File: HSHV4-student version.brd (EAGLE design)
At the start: 55 x 55 mm, 34 parts, among them IC1 DS3231, IC4 IO_EXPANDER, K1 PIN20X2, Q1 MOSFET-NCHANNEL2N7000, Q2 MOSFET-NCHANNEL2N7000, U1 256K_EEPROM

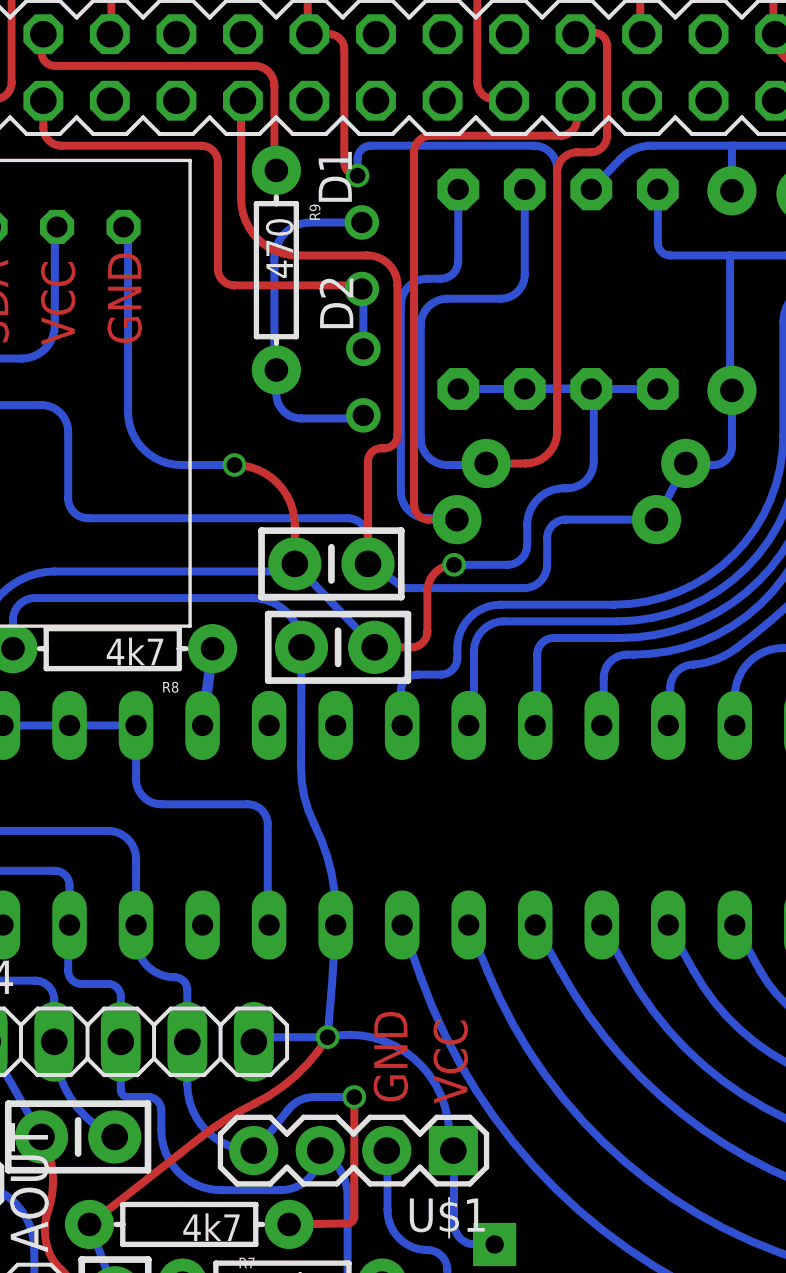
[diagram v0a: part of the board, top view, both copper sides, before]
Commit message: Increased size of via's for easier soldering
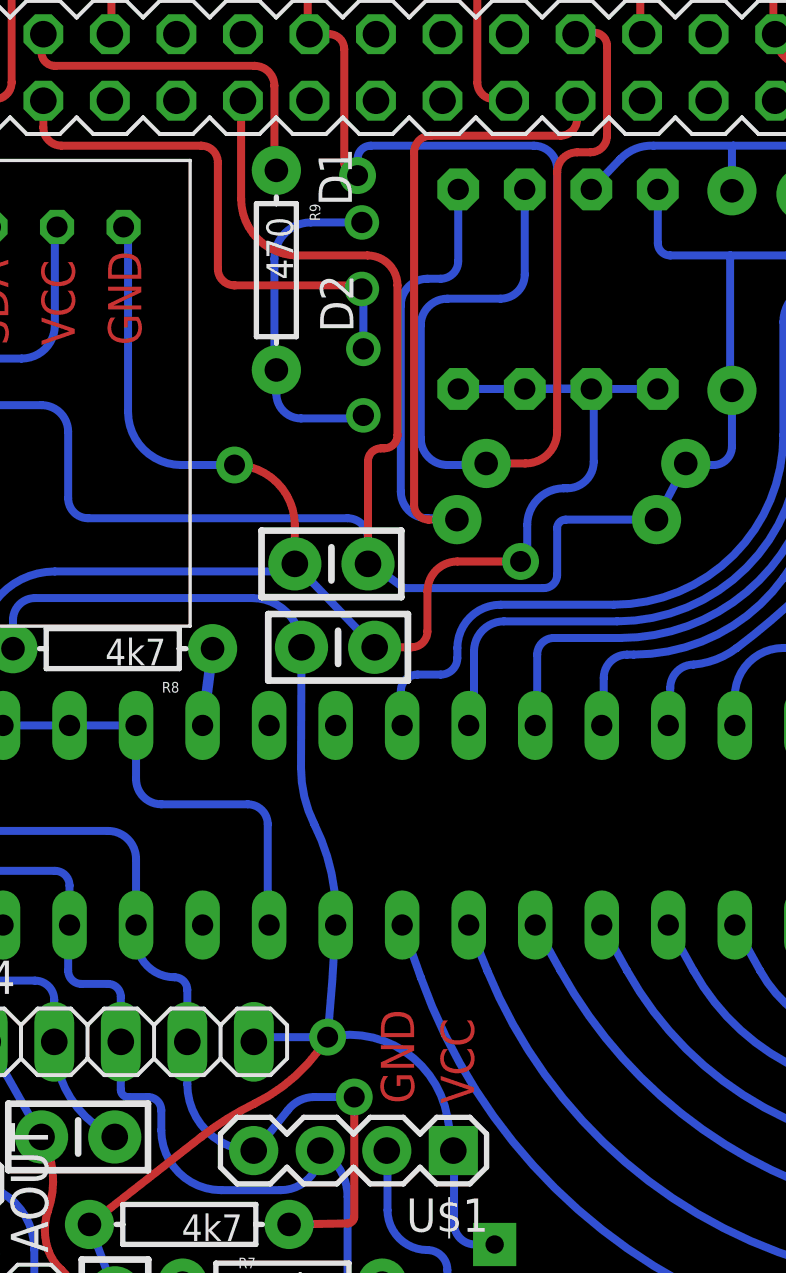
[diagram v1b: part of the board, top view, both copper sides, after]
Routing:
- net GND: track 297.6 -> 298.3 mm
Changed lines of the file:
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@@
 <setting verticaltext="up"/>
 </settings>
-<grid distance="0.01" unitdist="inch" unit="inch" style="lines" multiple="8" display="yes" altdistance="0.005" altunitdist="inch" altunit="inch"/>
+<grid distance="0.01" unitdist="inch" unit="mm" style="lines" multiple="8" display="yes" altdistance="0.005" altunitdist="inch" altunit="mm"/>
 <layers>
 <layer number="1" name="Top" color="4" fill="1" visible="yes" active="yes"/>
@@
 <text x="17.272" y="40.894" size="1.27" layer="1" rot="R90">VCC</text>
 <text x="19.812" y="40.894" size="1.27" layer="1" rot="R90">GND</text>
-<text x="32.258" y="11.938" size="1.27" layer="1" rot="R90">VCC</text>
-<text x="29.972" y="11.938" size="1.27" layer="1" rot="R90">GND</text>
+<text x="32.512" y="11.938" size="1.27" layer="1" rot="R90">VCC</text>
+<text x="30.226" y="11.938" size="1.27" layer="1" rot="R90">GND</text>
 </plain>
 <attributes>
@@
 <param name="rlMinPadBottom" value="10mil"/>
 <param name="rlMaxPadBottom" value="20mil"/>
-<param name="rlMinViaOuter" value="6mil"/>
+<param name="rlMinViaOuter" value="12mil"/>
 <param name="rlMaxViaOuter" value="20mil"/>
-<param name="rlMinViaInner" value="6mil"/>
+<param name="rlMinViaInner" value="10mil"/>
 <param name="rlMaxViaInner" value="20mil"/>
 <param name="rlMinMicroViaOuter" value="4mil"/>
@@
 <wire x1="28.575" y1="48.514" x2="28.067" y2="48.006" width="0.3048" layer="16" curve="90"/>
 <wire x1="28.067" y1="48.006" x2="28.067" y2="47.371" width="0.3048" layer="16"/>
-<via x="28.067" y="47.371" extent="1-16" drill="0.6"/>
+<via x="28.067" y="47.371" extent="1-16" drill="0.8"/>
 <wire x1="28.067" y1="47.371" x2="27.559" y2="47.879" width="0.3048" layer="1" curve="-90"/>
 <wire x1="27.559" y1="47.879" x2="27.559" y2="52.197" width="0.3048" layer="1"/>
@@
 <wire x1="36.068" y1="35.433" x2="35.941" y2="35.433" width="0.3048" layer="16"/>
 <wire x1="35.941" y1="35.433" x2="34.544" y2="34.036" width="0.3048" layer="16" curve="90"/>
-<wire x1="34.544" y1="34.036" x2="34.544" y2="33.274" width="0.3048" layer="16"/>
-<wire x1="34.544" y1="33.274" x2="33.782" y2="32.512" width="0.3048" layer="16" curve="-90"/>
-<wire x1="33.782" y1="32.512" x2="31.75" y2="32.512" width="0.3048" layer="16"/>
-<via x="31.75" y="32.512" extent="1-16" drill="0.6"/>
-<wire x1="31.75" y1="32.512" x2="30.734" y2="31.496" width="0.3048" layer="1" curve="90"/>
+<wire x1="33.782" y1="32.512" x2="34.29" y2="32.639" width="0.3048" layer="16"/>
+<via x="34.29" y="32.639" extent="1-16" drill="0.8"/>
 <wire x1="30.734" y1="31.496" x2="30.734" y2="29.972" width="0.3048" layer="1"/>
 <wire x1="30.734" y1="29.972" x2="30.124" y2="29.362" width="0.3048" layer="1" curve="-90"/>
@@
 <wire x1="19.304" y1="38.354" x2="21.336" y2="36.322" width="0.3048" layer="16" curve="90"/>
 <wire x1="21.336" y1="36.322" x2="23.368" y2="36.322" width="0.3048" layer="16"/>
-<via x="23.368" y="36.322" extent="1-16" drill="0.6"/>
+<via x="23.368" y="36.322" extent="1-16" drill="0.8"/>
 <wire x1="23.368" y1="36.322" x2="25.672" y2="34.018" width="0.3048" layer="1" curve="-90"/>
 <wire x1="25.672" y1="34.018" x2="25.672" y2="32.548" width="0.3048" layer="1"/>
@@
 <wire x1="16.764" y1="5.588" x2="17.272" y2="4.572" width="0.3048" layer="1" curve="-43.391833"/>
 <wire x1="17.272" y1="4.572" x2="18.806" y2="1.923" width="0.3048" layer="1" curve="50.41082"/>
+<wire x1="30.734" y1="31.496" x2="31.877" y2="32.639" width="0.3048" layer="1" curve="-90"/>
+<wire x1="31.877" y1="32.639" x2="34.29" y2="32.639" width="0.3048" layer="1"/>
+<wire x1="34.544" y1="34.036" x2="34.544" y2="32.893" width="0.3048" layer="16"/>
+<wire x1="34.544" y1="32.893" x2="34.29" y2="32.639" width="0.3048" layer="16" curve="-90"/>
 </signal>
 <signal name="+3V3">
@@
 <wire x1="11.684" y1="25.273" x2="11.684" y2="32.004" width="0.3048" layer="16"/>
 <wire x1="28.448" y1="32.639" x2="29.845" y2="31.623" width="0.3048" layer="16"/>
-<wire x1="29.845" y1="31.623" x2="34.417" y2="31.623" width="0.3048" layer="16"/>
-<wire x1="34.417" y1="31.623" x2="35.306" y2="32.512" width="0.3048" layer="16" curve="90"/>
-<wire x1="35.306" y1="32.512" x2="35.306" y2="33.528" width="0.3048" layer="16"/>
-<wire x1="35.306" y1="33.528" x2="36.015" y2="34.237" width="0.3048" layer="16" curve="-90"/>
 <wire x1="36.015" y1="34.237" x2="39.48" y2="34.237" width="0.3048" layer="16"/>
 <wire x1="3.37" y1="50.23" x2="3.37" y2="48.328" width="0.3048" layer="1"/>
@@
 <wire x1="13.589" y1="16.637" x2="12.573" y2="17.653" width="0.3048" layer="16" curve="-90"/>
 <wire x1="16.487" y1="14.299" x2="18.796" y2="10.668" width="0.3048" layer="16" curve="64.905625"/>
+<wire x1="36.015" y1="34.237" x2="35.687" y2="33.909" width="0.3048" layer="16" curve="90"/>
+<wire x1="35.687" y1="33.909" x2="35.687" y2="32.131" width="0.3048" layer="16"/>
+<wire x1="35.687" y1="32.131" x2="35.179" y2="31.623" width="0.3048" layer="16" curve="-90"/>
+<wire x1="35.179" y1="31.623" x2="29.845" y2="31.623" width="0.3048" layer="16"/>
 </signal>
 <signal name="SCL0-3">
@@
 <wire x1="22.098" y1="10.668" x2="24.13" y2="11.938" width="0.3048" layer="1" curve="-12.106495"/>
 <wire x1="24.13" y1="11.938" x2="26.924" y2="14.478" width="0.3048" layer="1" curve="32.643116"/>
-<via x="26.924" y="14.478" extent="1-16" drill="0.6"/>
+<via x="26.924" y="14.478" extent="1-16" drill="0.8"/>
 <wire x1="26.924" y1="14.478" x2="24.107" y2="14.478" width="0.3048" layer="16"/>
 <wire x1="24.107" y1="14.478" x2="24.107" y2="14.299" width="0.3048" layer="16"/>
@@
 <wire x1="27.686" y1="7.366" x2="27.94" y2="7.62" width="0.3048" layer="1" curve="90"/>
 <wire x1="27.94" y1="7.62" x2="27.94" y2="12.192" width="0.3048" layer="1"/>
-<via x="27.94" y="12.192" extent="1-16" drill="0.6"/>
+<via x="27.94" y="12.192" extent="1-16" drill="0.8"/>
 <wire x1="27.94" y1="12.192" x2="26.416" y2="12.192" width="0.3048" layer="16"/>
 <wire x1="26.416" y1="12.192" x2="25.4" y2="11.684" width="0.3048" layer="16" curve="53.130102"/>

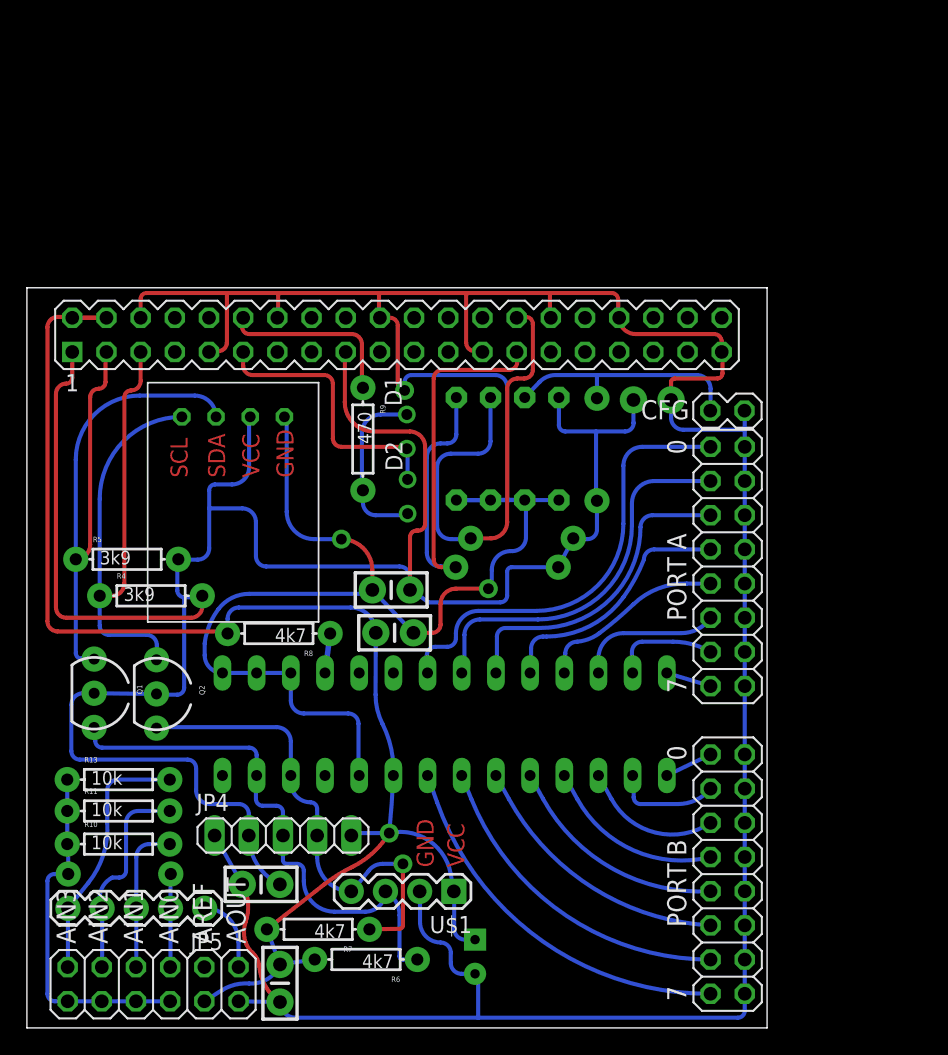
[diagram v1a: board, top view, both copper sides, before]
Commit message: Made larger pads
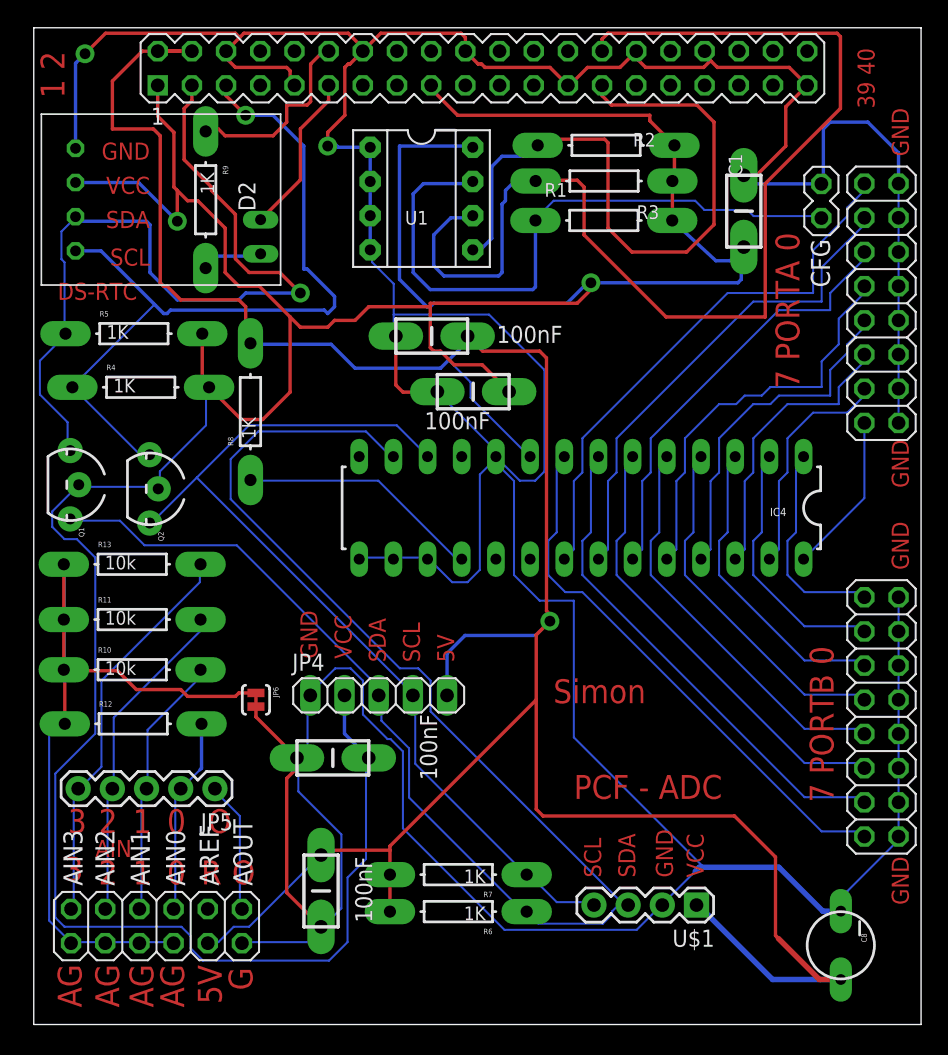
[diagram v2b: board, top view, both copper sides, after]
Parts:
- removed D1: (no value), SparkFun-LED:LED3MM-NS
- added JP6: JUMPER-PAD-2-NC_BY_TRACE, SparkFun-Passives:PAD-JUMPER-2-NC_BY_TRACE_YES_SILK
- R1, R2, R4, R5: value 3k9 -> 1K
- R6, R7, R8: value 4k7 -> 1K
- R9: value 470 -> 1K
- moved R2 32.2 mm to (43.0, 65.6), flipped to the top, turned to 0 degrees
- moved R1 27.2 mm to (42.9, 62.9), flipped to the top, turned to 0 degrees
- moved C8 27.2 mm to (60.5, 6.14), flipped to the top, turned to 270 degrees
- moved JP1 22.7 mm to (63.5, 53.8)
- moved C5 22.2 mm to (30.1, 51.4), turned to 0 degrees
- moved D2 22.2 mm to (17.4, 58.8)
- moved R9 21.3 mm to (13.3, 61.5)
- moved K1 20.8 mm to (33.9, 71.3)
- moved IC1 19.9 mm to (3.61, 61.6), turned to 270 degrees
- moved U1 19.7 mm to (29.3, 61.6), flipped to the top, turned to 270 degrees
- moved IC4 19.0 mm to (41.2, 38.6), flipped to the top, turned to 180 degrees
- moved U$1 18.1 mm to (49.8, 9.13)
- moved R3 17.0 mm to (42.9, 60.0), flipped to the top, turned to 0 degrees
- moved R5 16.8 mm to (7.95, 51.6)
- moved R8 16.6 mm to (16.6, 45.8), turned to 90 degrees
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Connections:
- net AGND: now also JP6.1
- net GND: now also JP6.2
- net GPIO17: no longer D1.A
- net N$2: no longer D1.K
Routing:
- net +3V3: track 168.8 -> 259.1 mm, vias 0 -> 2
- net +5V: track 108.9 -> 198.6 mm
- net SDA1-5: track 39.5 -> 118.7 mm
- net GND: track 298.3 -> 373.3 mm, vias 3 -> 2
- net SCL0-3: track 35.8 -> 85.5 mm
- net SCL1-5: track 35.3 -> 70.4 mm, vias 1 -> 0
- net AGND: track 26.5 -> 60.4 mm
- net N$3: track 18.2 -> 47.9 mm
- net SDA1-3: track 45.3 -> 61.9 mm, vias 0 -> 1
- net SCL1-3: track 43.9 -> 59.2 mm, vias 0 -> 1
- net N$15: track 2.96 -> 18.2 mm
- net N$27: track 19.7 -> 33.9 mm
- net N$28: track 23.3 -> 37.5 mm
- net N$29: track 26.9 -> 41.1 mm
- net N$26: track 16.2 -> 30.3 mm
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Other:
- board size 55 x 55 mm -> 65.9 x 74.1 mm
- board text added: "1"
- board text added: "1 2"
- board text added: "2"
- board text added: "3"
- board text added: "39 40"
- board text added: "5V"
- board text added: "7 PORTA 0"
- board text added: "7 PORTB 0"
- board text added: "AG"
- board text added: "AIN"
- board text added: "DS-RTC"
- board text added: "G"
- board text added: "O"
- board text added: "PCF - ADC"
- board text added: "R"
- board text added: "Simon"
- board text removed: "7"
- board text removed: "PORT A"
- board text removed: "PORT B"
